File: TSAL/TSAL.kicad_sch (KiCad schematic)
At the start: 57 parts, among them J6 Conn_01x02, J7 Conn_02x03_Counter_Clockwise, J8 Conn_02x01, J9 Conn_02x01, Q4 BSS138, Q5 BSS138, Q6 AO3401A, U10 74HC27, U11 LM339, U12 74HC74, U13 LM7805_TO220, U4 LM358, U5 4N35, U6 LM339, U7 74HC20, U8 74HC86, U9 74HC08

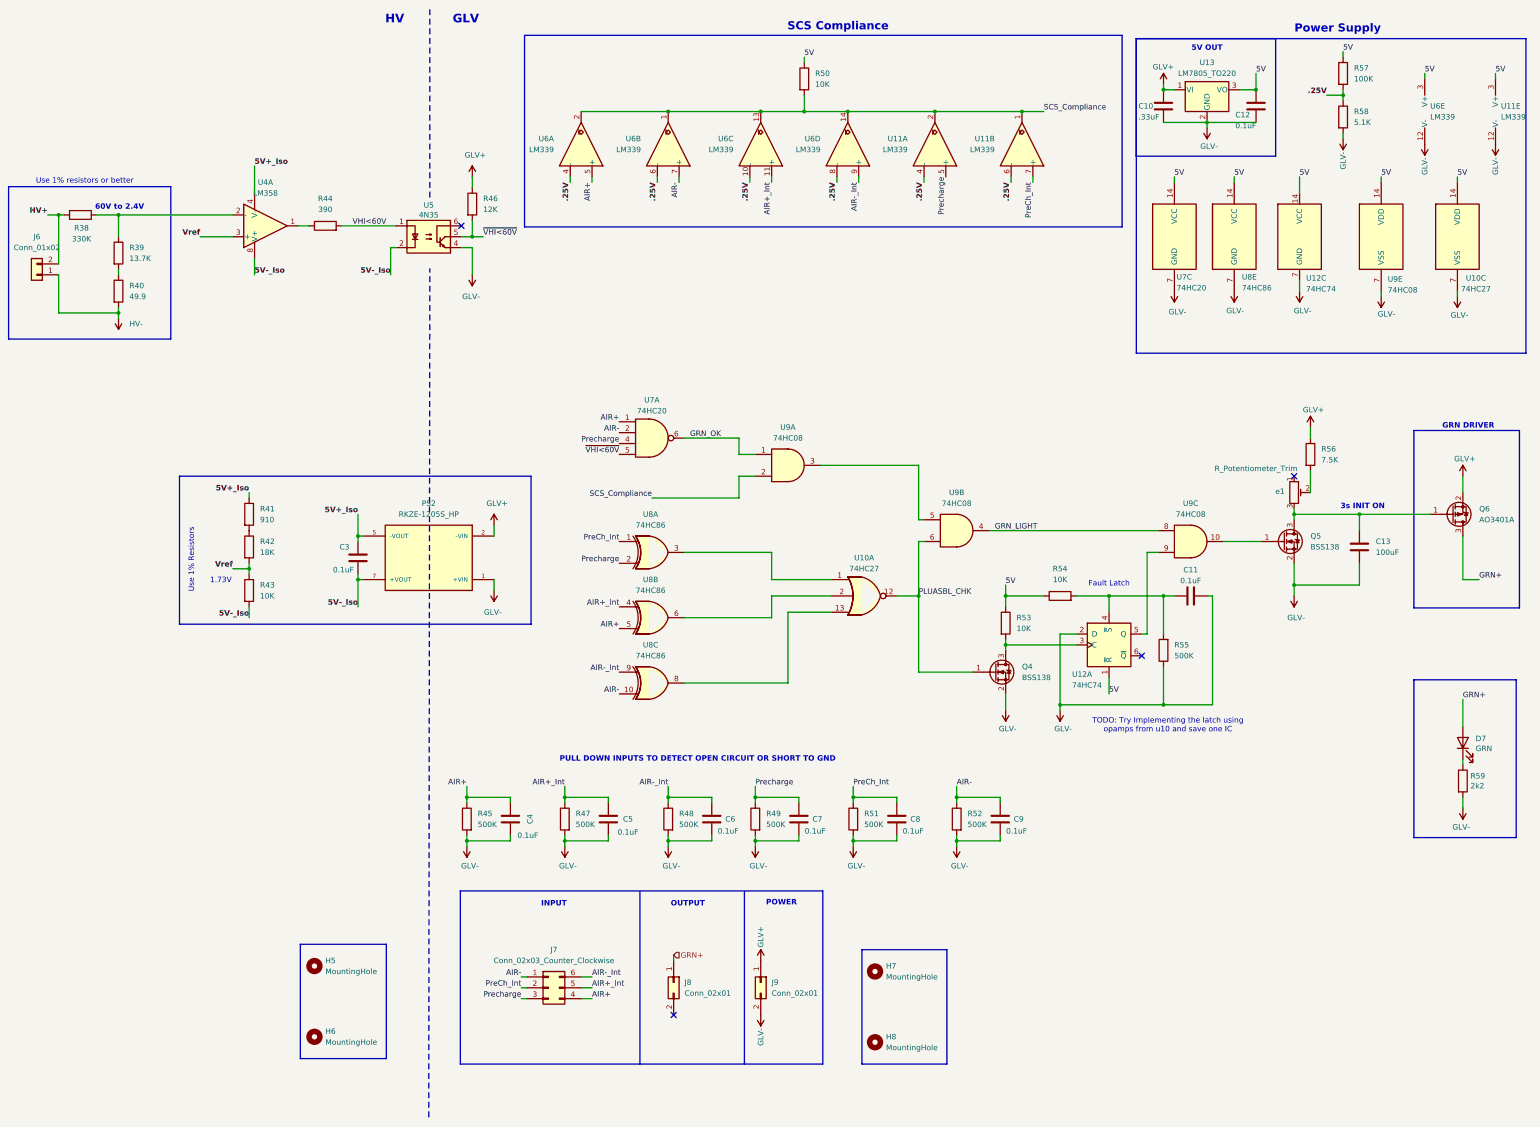
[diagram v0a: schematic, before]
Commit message: Precharge: cap DC bias correction, PDs on TSAL
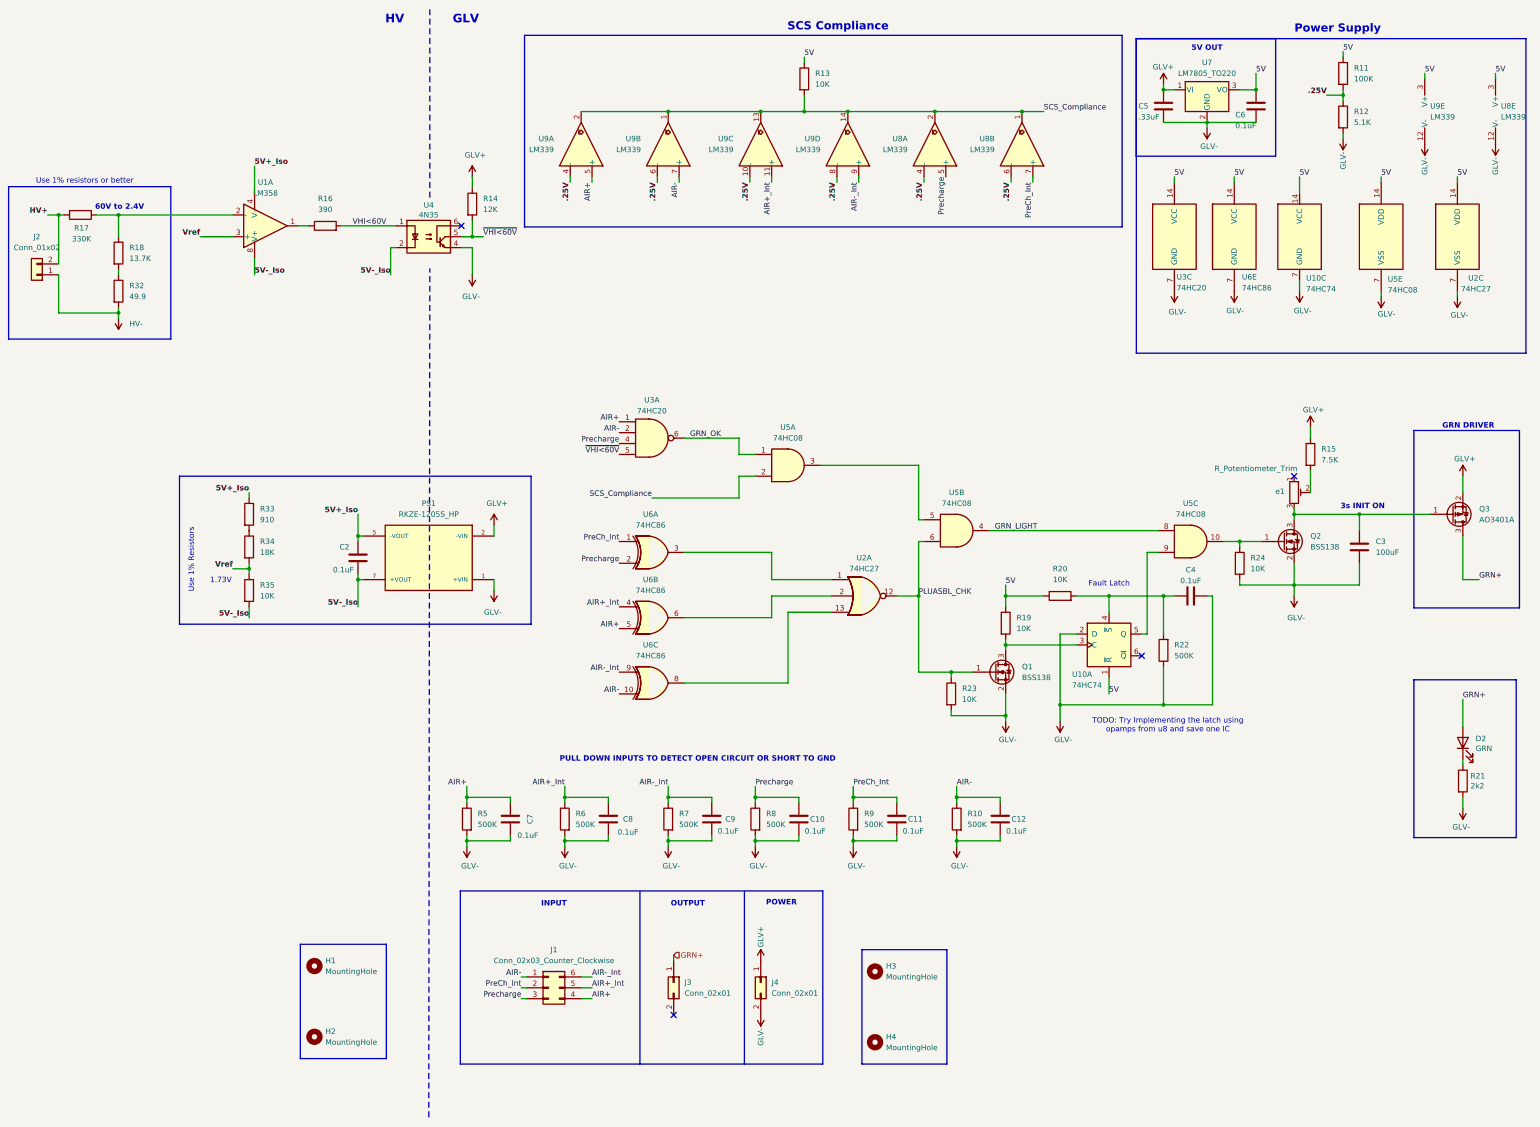
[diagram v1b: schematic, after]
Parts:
- added R23, R24: 10K, Resistor_SMD:R_0603_1608Metric_Pad0.98x0.95mm_HandSolder, symbol Device:R
- renumbered C7 to C10, C8 to C11, C9 to C12, C3 to C2, C13 to C3, C11 to C4, C10 to C5, C12 to C6, C4 to C7, C5 to C8, C6 to C9, D7 to D2, H5 to H1, H6 to H2, H7 to H3, H8 to H4, J7 to J1, J6 to J2, J8 to J3, J9 to J4, PS2 to PS1, Q4 to Q1, Q5 to Q2, Q6 to Q3, R52 to R10, R57 to R11, R58 to R12, R50 to R13, R46 to R14, R56 to R15, R44 to R16, R38 to R17, R39 to R18, R53 to R19, R54 to R20, R59 to R21, R55 to R22, R40 to R32, R41 to R33, R42 to R34, R43 to R35, R45 to R5, R47 to R6, R48 to R7, R49 to R8, R51 to R9, U4 to U1, U12 to U10, U10 to U2, U7 to U3, U5 to U4, U9 to U5, U8 to U6, U13 to U7, U11 to U8, U6 to U9
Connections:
- net GLV-: now also R23.2, R24.2
- net PLUASBL_CHK: now also R23.1
- net at Q2.1 (G), U5.10: now also R24.1
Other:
- note added: "TODO: Try Implementing the latch using opamps from u8 and save one IC"
- note removed: "TODO: Try Implementing the latch using opamps from u10 and save one IC"
